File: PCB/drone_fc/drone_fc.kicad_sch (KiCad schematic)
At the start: 2 parts, among them U1 nRF52840

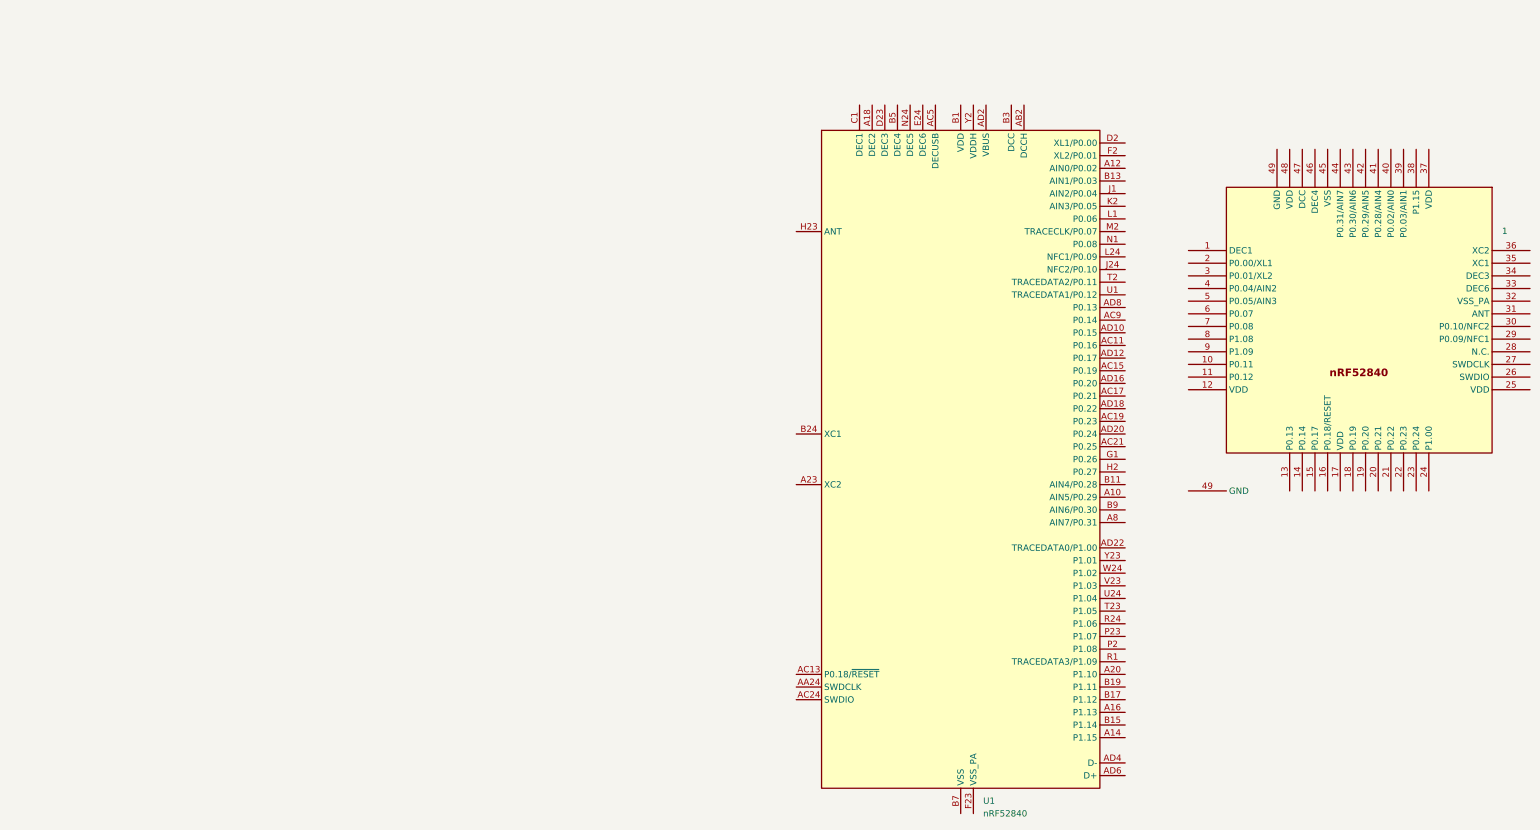
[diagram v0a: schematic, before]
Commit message: Starting a PCB with the nRF52840. The Nordic-provided boards crash KiCAD so I'm making it myself I guess
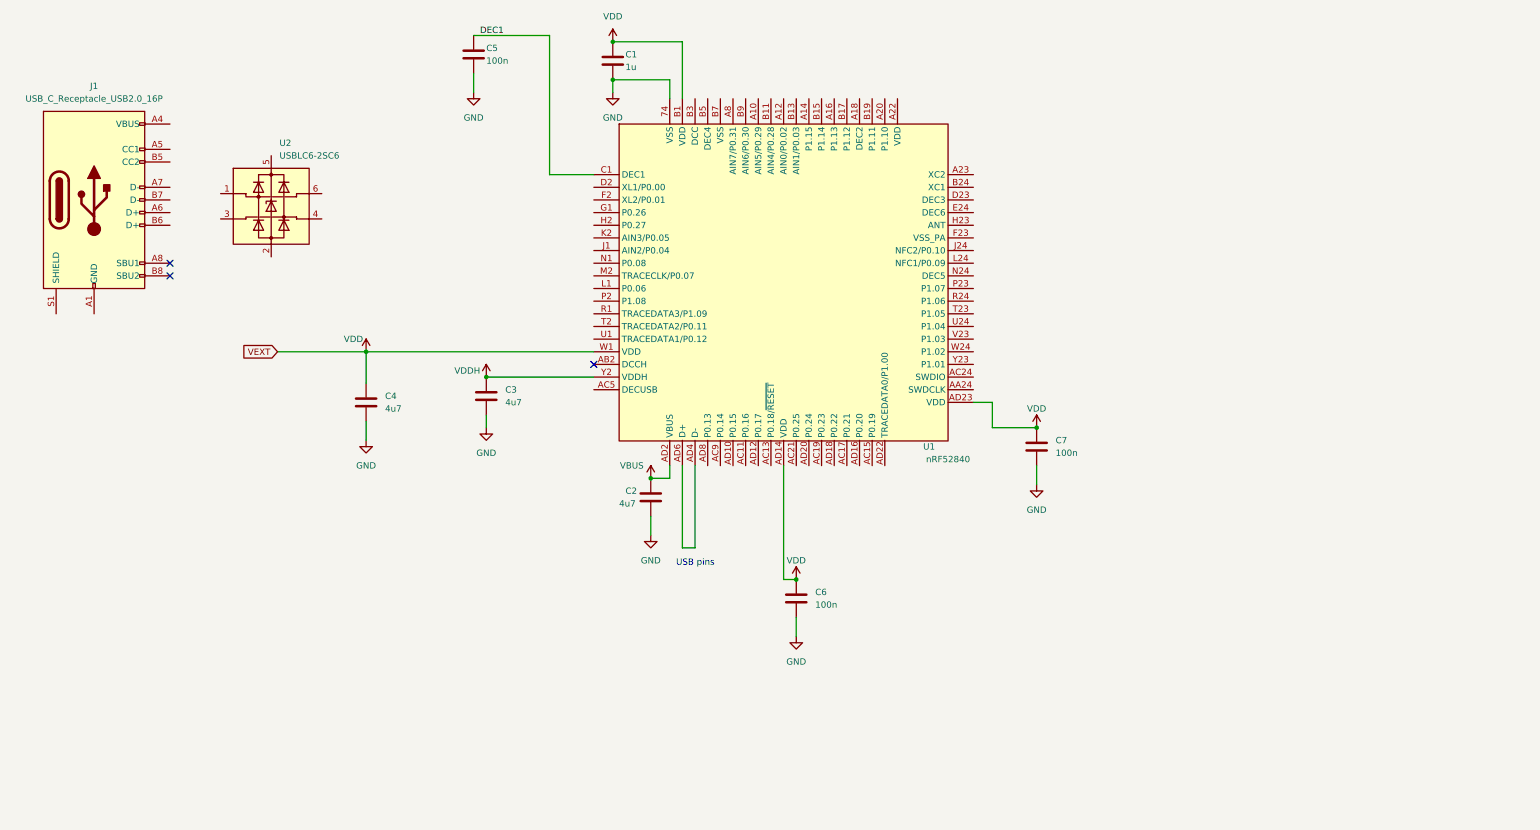
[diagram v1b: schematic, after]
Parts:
- removed 1: ~, symbol drone_fc-altium-import:root_0_nRF52840_QFAA
- removed U1: nRF52840, Package_DFN_QFN:Nordic_AQFN-73-1EP_7x7mm_P0.5mm, symbol MCU_Nordic:nRF52840
- added C1: 1u, symbol Device:C
- added C2, C3, C4: 4u7, symbol Device:C
- added C5, C6, C7: 100n, symbol Device:C
- added J1: USB_C_Receptacle_USB2.0_16P, symbol Connector:USB_C_Receptacle_USB2.0_16P
- added U1: nRF52840, Package_DFN_QFN:Nordic_AQFN-73-1EP_7x7mm_P0.5mm, symbol nRF52840:nRF52840
- added U2: USBLC6-2SC6, Package_TO_SOT_SMD:SOT-23-6, symbol STM32_PhilsLab_SchSym:USBLC6-2SC6
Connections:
- new net: J1.A1 (GND), J1.A12 (GND), J1.B1 (GND), J1.B12 (GND)
- new net: J1.A4 (VBUS), J1.A9 (VBUS), J1.B4 (VBUS), J1.B9 (VBUS)
- new net: U1.AD4 (D-), U1.AD6 (D+)
- new net DEC1: C5.1, U1.C1 (DEC1)
- new net GND: C1.2, C2.2, C3.2, C4.2, C5.2, C6.2, C7.2, U1.74 (VSS)
- new net VBUS: C2.1, U1.AD2 (VBUS)
- new net VDD: C1.1, C4.1, C6.1, C7.1, U1.AD14 (VDD), U1.AD23 (VDD), U1.B1 (VDD), U1.W1 (VDD)
- new net VDDH: C3.1, U1.Y2 (VDDH)
- no-connect marks 0 -> 3
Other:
- note added: "USB pins"

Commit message: Finished basic configuration schematic for nRF52840 and added USB receptacle and ESD protection
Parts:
- added BT1: Battery, symbol Device:Battery
- added C10, C14, C18: NC, symbol Device:C
- added C11: 100p, symbol Device:C
- added C12, C13: 12p, symbol Device:C
- added C15, C9: 1u, symbol Device:C
- added C16: 0p8, symbol Device:C
- added C17: 0p5, symbol Device:C
- added C8: 4u7, symbol Device:C
- added L1: 4n7, symbol Device:L
- added R1, R2: R, symbol Device:R
- added U3: BNO055, Package_LGA:LGA-28_5.2x3.8mm_P0.5mm, symbol Sensor_Motion:BNO055
- added X1: 32MHz, symbol Device:Crystal_Small
- U1: footprint Package_DFN_QFN:Nordic_AQFN-73-1EP_7x7mm_P0.5mm -> nRF52840:nRF52840
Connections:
- net VDD is gone; now on net +15V: C1.1, C4.1, C6.1, C7.1, U1.AD14 (VDD), U1.AD23 (VDD), U1.B1 (VDD), U1.W1 (VDD)
- net GND: now also J1.A1 (GND), J1.A12 (GND), J1.B1 (GND), J1.B12 (GND), U1.B7 (VSS), U1.F23 (VSS_PA), U2.2 (GND), BT1.2 (-), C10.2, C11.2, C12.2, C13.2, C14.2, C15.2, C16.1, C17.1, C18.1, C8.2, C9.2, R1.2, R2.2
- net VBUS: now also J1.A4 (VBUS), J1.A9 (VBUS), J1.B4 (VBUS), J1.B9 (VBUS)
- net at J1.A5 (CC1): now also R2.1
- net DR+: now reaches J1.A6 (D+)
- net DR+: now also J1.B6 (D+), U2.6 (I/O1)
- net DR-: now reaches J1.A7 (D-)
- net DR-: now also J1.B7 (D-), U2.4 (I/O2)
- net at J1.B5 (CC2): now also R1.1
- net D+: now reaches U2.1 (I/O1)
- net D+: now also U1.AD6 (D+)
- net D-: now reaches U2.3 (I/O2)
- net D-: now also U1.AD4 (D-)
- net +15V: now reaches U2.5 (VBUS)
- net +15V: now also U1.A22 (VDD), BT1.1 (+), C15.1
- net at U1.A18 (DEC2): now also C14.1
- net at U1.A23 (XC2): now also C13.1, X1.2
- net at U1.AC5 (DECUSB): now also C8.1
- net at U1.B24 (XC1): now also C12.1, X1.1
- net DEC4_6: now reaches U1.B5 (DEC4)
- net DEC4_6: now also U1.E24 (DEC6), C10.1, C9.1
- net DEC3: now reaches U1.D23 (DEC3)
- net DEC3: now also C11.1
- net at U1.H23 (ANT): now also C16.2, L1.1
- new net: U3.15 (GNDIO), U3.16 (GNDIO), U3.25 (GNDIO)
- new net RF: C17.2, C18.2, L1.2
- no-connect marks 3 -> 5
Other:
- note added: "6S Battery"
- note added: "BNO055 9-axis sensor"
- note added: "May not get used until later"
- note added: "Voltage Reg goes here"
- note removed: "USB pins"
- moved on the sheet: C1, C2, C3, C4, C5, C6, C7, U1, U2

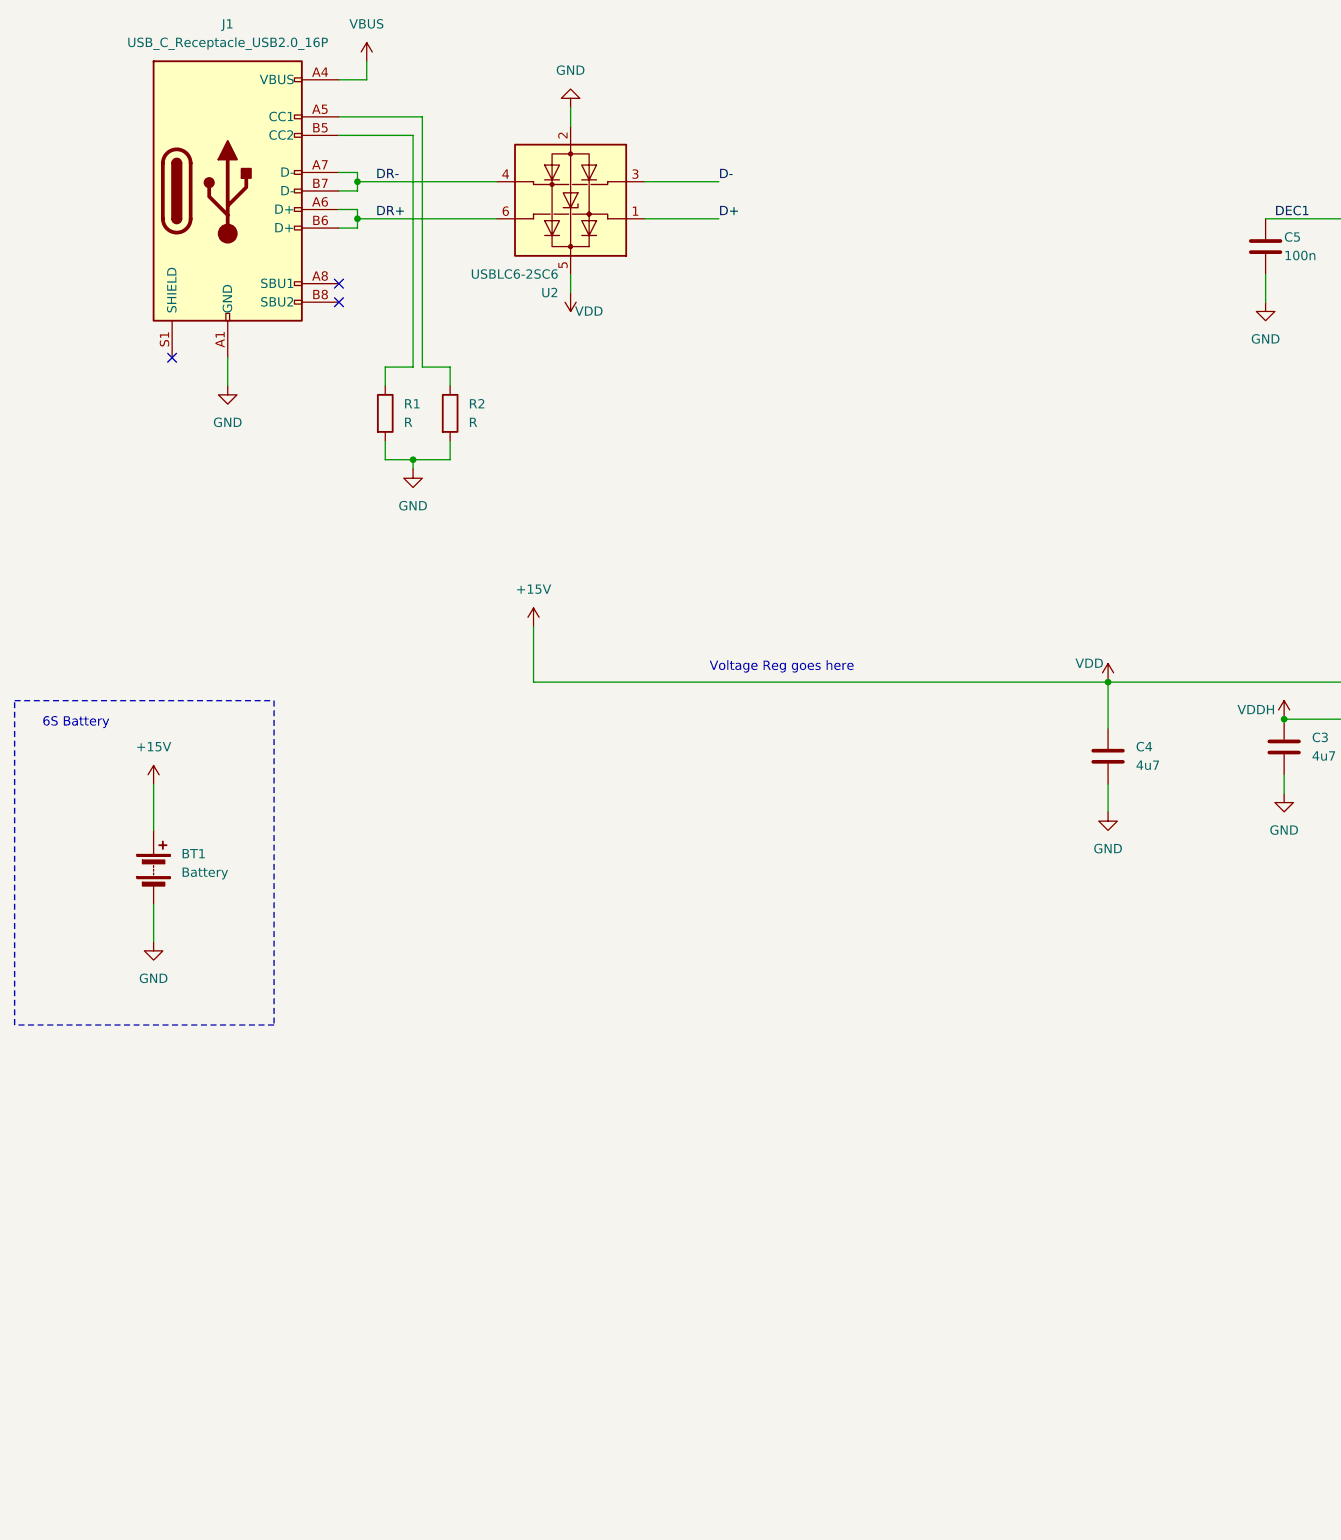
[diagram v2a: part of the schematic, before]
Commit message: Added voltage regulator after hours of thinking about it too hard
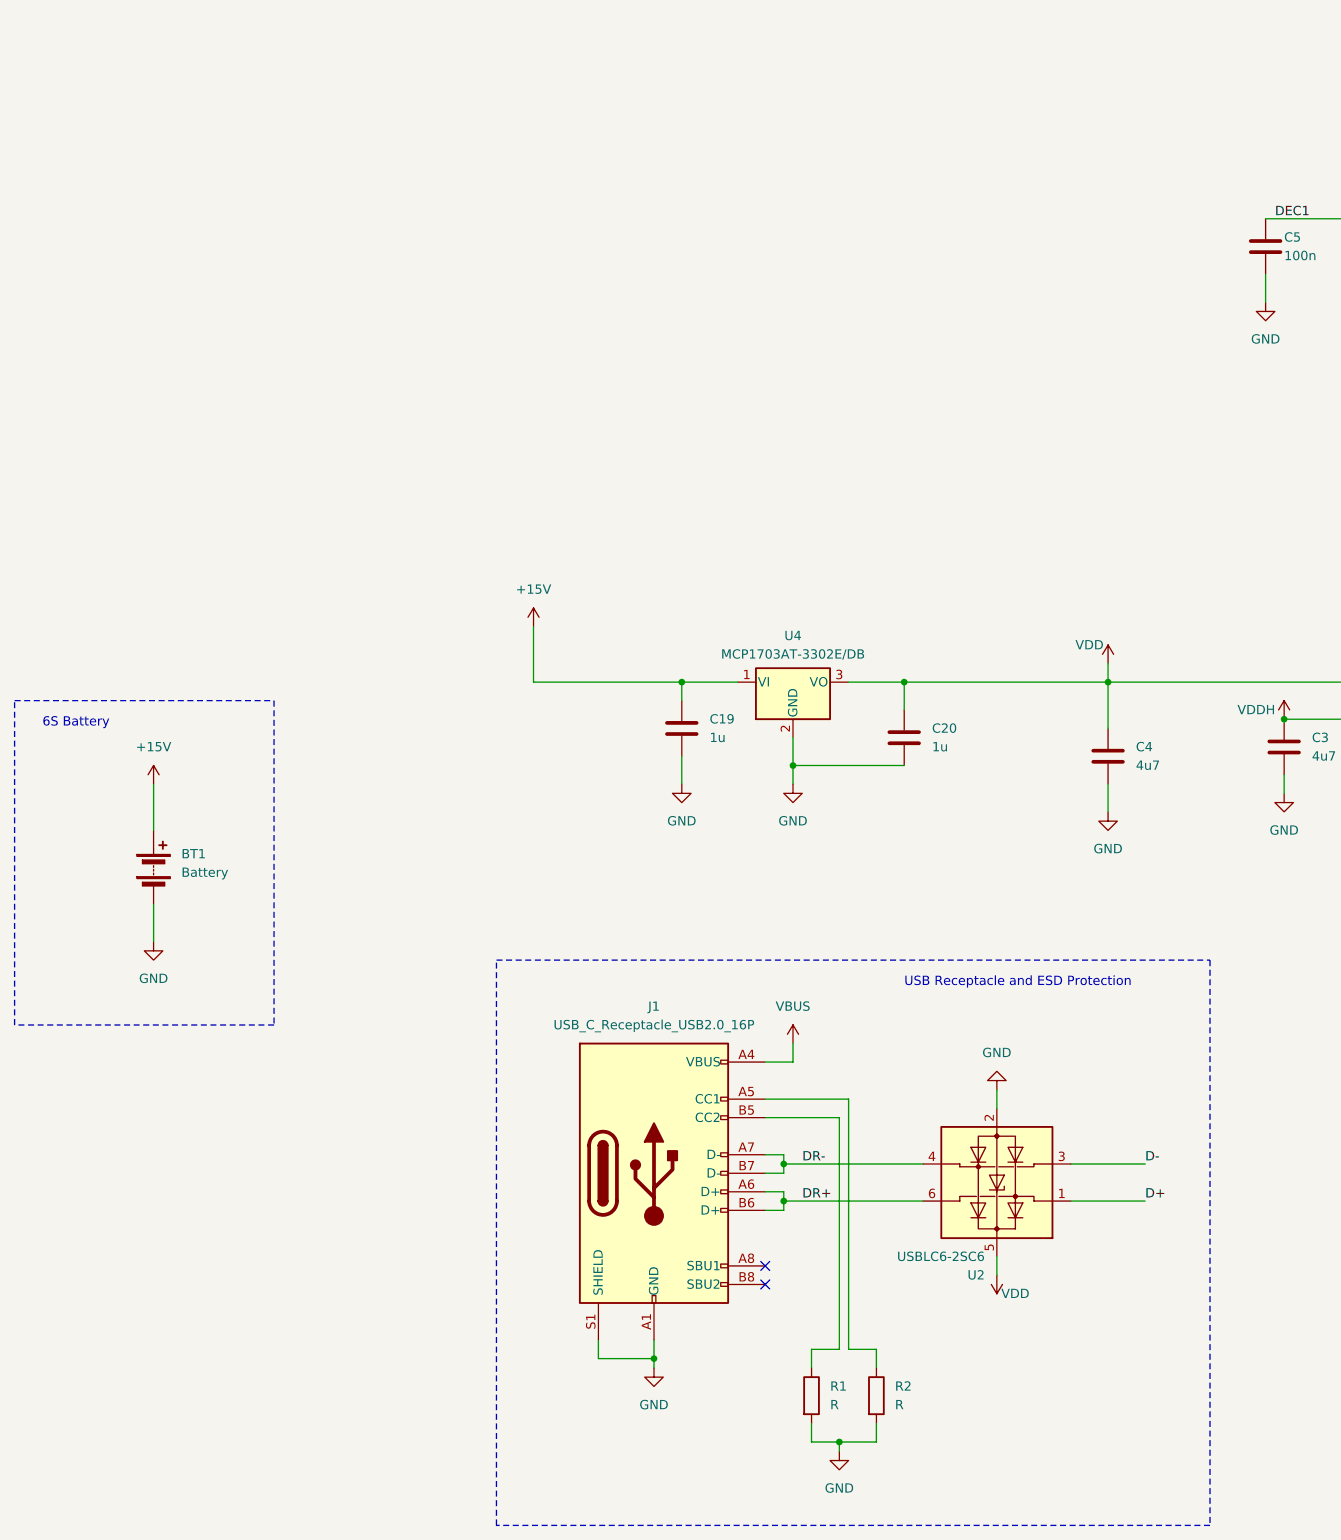
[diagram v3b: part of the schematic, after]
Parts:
- added C19, C20: 1u, symbol Device:C
- added U4: MCP1703AT-3302E/DB, Package_TO_SOT_SMD:SOT-223-3_TabPin2, symbol Regulator_Linear:MCP1703Ax-330xxDB
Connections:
- net +15V: now also C19.1, U4.1 (VI); no longer C1.1, C15.1, C4.1, C6.1, C7.1, U1.A22 (VDD), U1.AD14 (VDD), U1.AD23 (VDD), U1.B1 (VDD), U1.W1 (VDD), U2.5 (VBUS)
- net GND: now also J1.S1 (SHIELD), C19.2, C20.2, U4.2 (GND)
- new net VDD: C1.1, C15.1, C20.1, C4.1, C6.1, C7.1, U1.A22 (VDD), U1.AD14 (VDD), U1.AD23 (VDD), U1.B1 (VDD), U1.W1 (VDD), U2.5 (VBUS), U4.3 (VO)
- no-connect marks 5 -> 4
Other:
- note added: "USB Receptacle and ESD Protection"
- note removed: "Voltage Reg goes here"
- moved on the sheet: J1, R1, R2, U2

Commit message: Well the BNO055 isn't recommended for new projects, so I've replaced it with the ICM-20948, and updated the PCB's edge to hopefully match the ESC
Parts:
- removed U3: BNO055, Package_LGA:LGA-28_5.2x3.8mm_P0.5mm, symbol Sensor_Motion:BNO055
- added C21, C22: 0u1, symbol Device:C
- added J2: Conn_01x04_Socket, symbol Connector:Conn_01x04_Socket
- added J3: Conn_01x07_Socket, symbol Connector:Conn_01x07_Socket
- added R3, R4: 10k, symbol Device:R
- added U3: ICM-20948, Sensor_Motion:InvenSense_QFN-24_3x3mm_P0.4mm, symbol Sensor_Motion:ICM-20948
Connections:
- net GND: now also C21.2, C22.2, U3.18 (GND), U3.20 (GND)
- net VDD: now also C21.1, R3.1, R4.1, U3.13 (VDD)
- new net: C22.1, U3.10 (REGOUT)
- new net SCL: R3.2, U3.23 (SCL/SCLK)
- new net SDA: R4.2, U3.24 (SDA/SDI)
- no-connect marks 4 -> 7
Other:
- note added: "ICM-20948 IMU"
- note removed: "BNO055 9-axis sensor"
- moved on the sheet: C19, C20, C4, U4

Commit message: Routed out the nRF52840 so I could tell which pins were best for peripherals
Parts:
- removed C3: 4u7, symbol Device:C
- J1: footprint (none) -> Connector_USB:USB_C_Receptacle_GCT_USB4105-xx-A_16P_TopMnt_Horizontal; Link (none) -> https://www.digikey.com/en/products/detail/amphenol-cs-comm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; Manufacturer (none) -> Amphenol ICC (Commercial Products)
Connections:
- net VDDH is gone; now on net VBUS: U1.Y2 (VDDH)
- net GND: now also U3.11 (FSYNC)
- net IMU_INT: now reaches U3.12 (INT1)
- no-connect marks 7 -> 9
